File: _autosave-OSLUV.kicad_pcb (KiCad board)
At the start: 4 copper layers, 110 x 90 mm, 190 parts, among them IC1 NCP12510ASN65T1G, IC2 SFH6156-3, IC3 INA210, IC4 AP63300WU-7, IC5 AP63300WU-7, IC6 STM32G071KBT6, IC7 TLV9001IDBVR, IC8 FAN3100TSX, IC9 TLV1821, J1 B08B-XASK-1-A_LF__SN_, J2 TC2050-IDC, J3 BM02B-SRSS-TB_LF__SN_, J4 BM02B-SRSS-TB_LF__SN_, J5 640445-2, J6 640445-2, J7 B5P-VH, Q1 STD3NK80ZT4, Q2 BAT847B, Q3 BSS138, Q4 BC807, T1 750343466, T4 NMOS_GDS-KS_SMD, U1 OPA2356AIDGKR, U2 AZ431LANTR

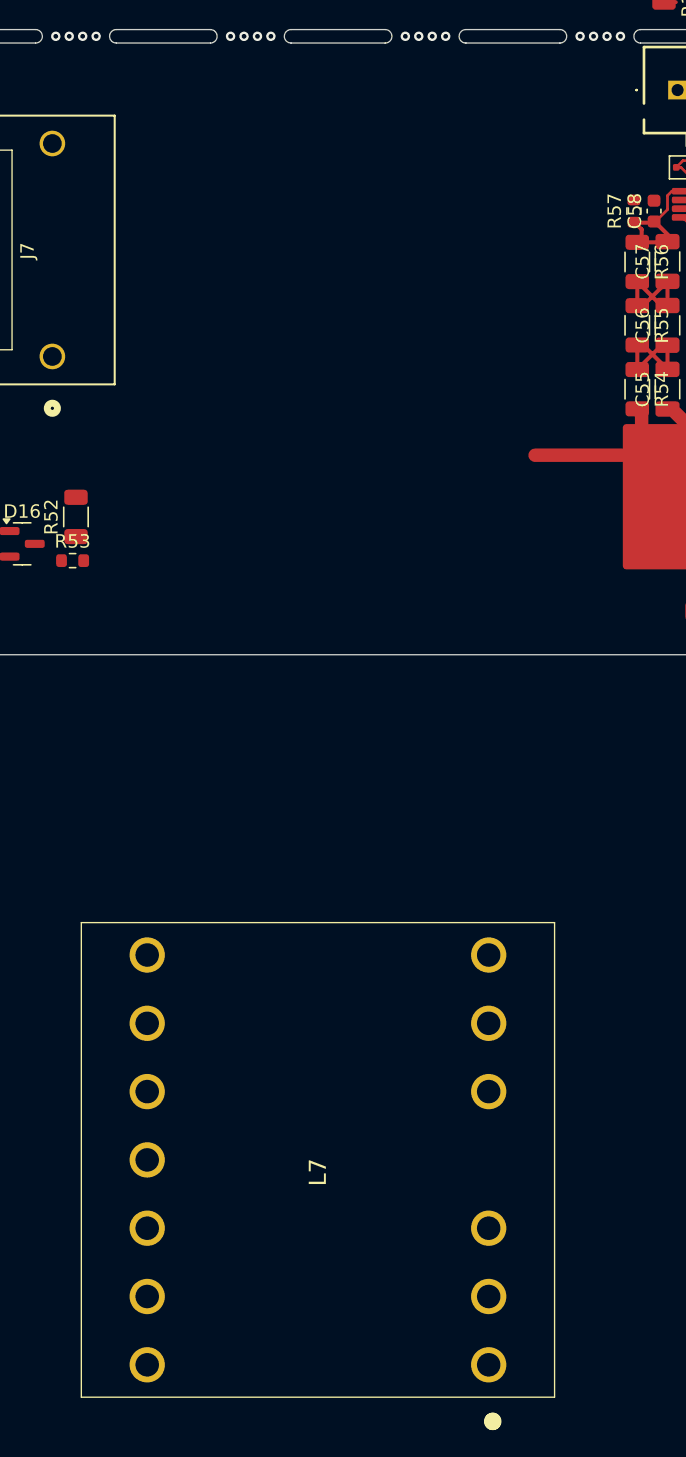
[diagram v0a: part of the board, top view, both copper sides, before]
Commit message: branch main, transfomer changed to EF25
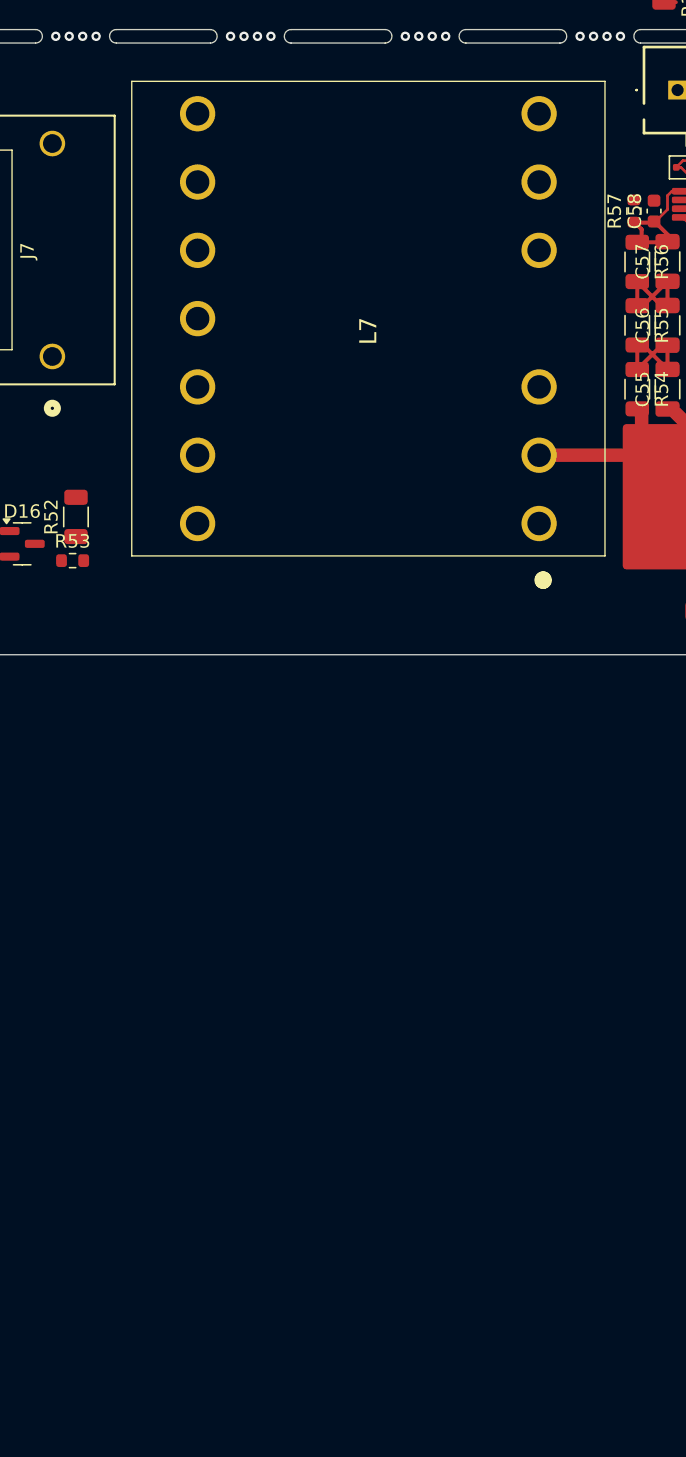
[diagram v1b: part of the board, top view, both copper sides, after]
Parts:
- moved L7 62.7 mm to (77.8, 115.0)
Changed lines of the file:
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@@
 	(footprint "Hansmann:B66359B1013T001"
 		(layer "F.Cu")
-		(at 74 177.575 90)
+		(at 77.75 115 90)
 		(descr "B66359B1013T001-2")
 		(tags "Inductor")
@@
 		)
 		(embedded_fonts no)
-		(model "${WE_3DMODEL_DIR}/Inductor_SMD_Wurth.3dshapes/L_Wurth_WE-LQ-1812.wrl"
+		(model "${KICAD9_3DMODEL_DIR}/Inductor_SMD_Wurth.3dshapes/L_Wurth_WE-LQ-1812.step"
 			(offset
 				(xyz 0 0 0)
